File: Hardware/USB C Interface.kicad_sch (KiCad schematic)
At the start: 5 parts

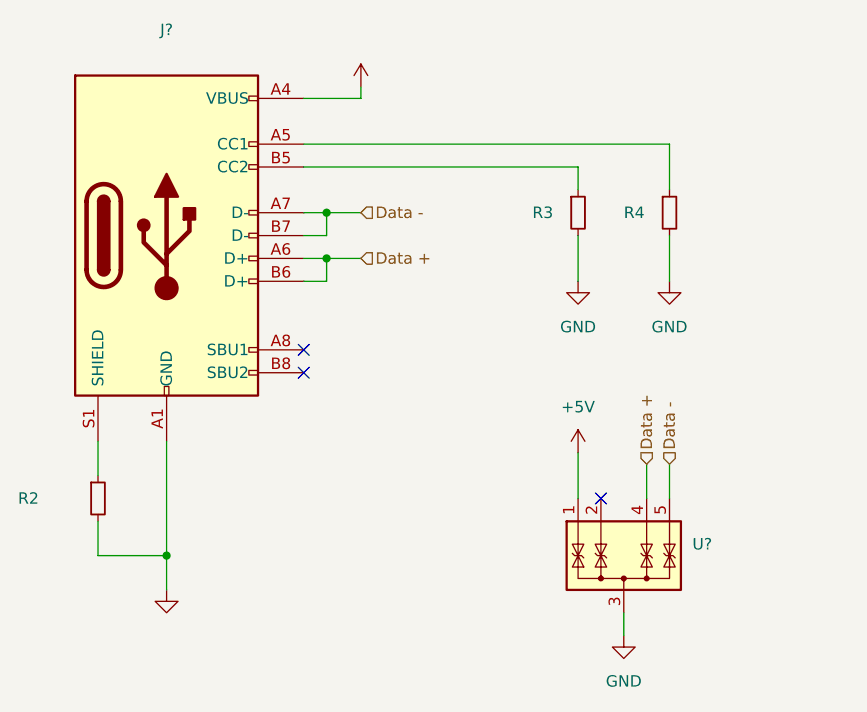
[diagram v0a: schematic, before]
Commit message: Add VL53L0X
Added VL53L0X range finders and reworked traces.
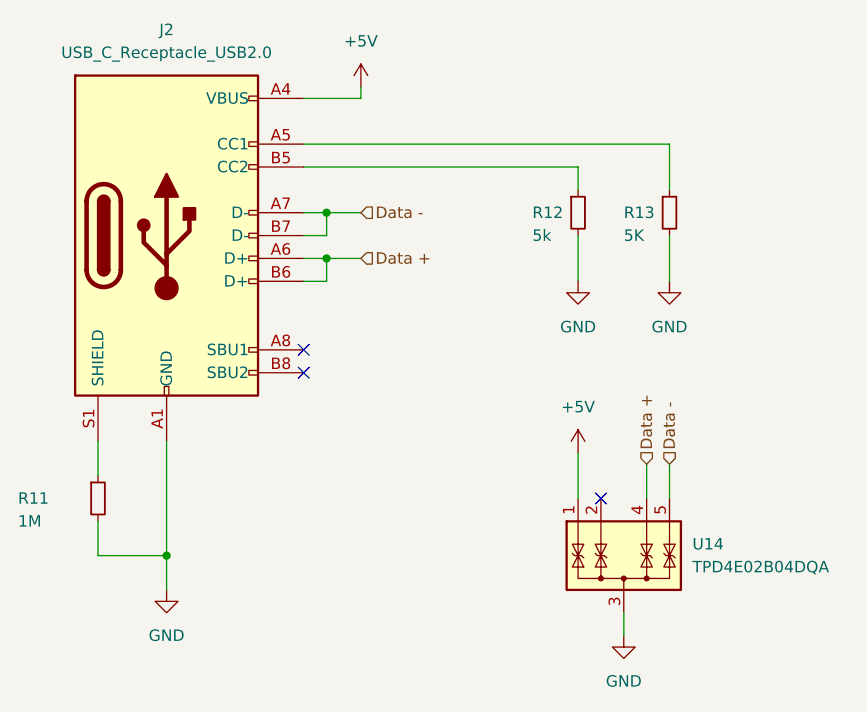
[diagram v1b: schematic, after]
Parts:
- J2: renamed from J?; value (none) -> USB_C_Receptacle_USB2.0; footprint (none) -> Connector_USB:USB_C_Receptacle_XKB_U262-16XN-4BVC11
- R11: renamed from R2; value (none) -> 1M; footprint (none) -> Resistor_SMD:R_0805_2012Metric
- R12: renamed from R3; value (none) -> 5k; footprint (none) -> Resistor_SMD:R_0805_2012Metric
- R13: renamed from R4; value (none) -> 5K; footprint (none) -> Resistor_SMD:R_0805_2012Metric
- U14: renamed from U?; value (none) -> TPD4E02B04DQA; footprint (none) -> Package_SON:USON-10_2.5x1.0mm_P0.5mm
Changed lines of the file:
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@@
   (symbol (lib_id "power:GND") (at 127 130.81 0) (unit 1)
     (in_bom yes) (on_board yes) (fields_autoplaced)
-    (property "Reference" "#PWR?" (id 0) (at 127 137.16 0)
+    (property "Reference" "#PWR059" (id 0) (at 127 137.16 0)
       (effects (font (size 1.27 1.27)) hide)
     )
-    (property "Value" "" (id 1) (at 127 135.89 0))
+    (property "Value" "GND" (id 1) (at 127 135.89 0))
     (property "Footprint" "" (id 2) (at 127 130.81 0)
       (effects (font (size 1.27 1.27)) hide)
@@
   (symbol (lib_id "Device:R_Small") (at 119.38 120.65 0) (unit 1)
     (in_bom yes) (on_board yes)
-    (property "Reference" "R2" (id 0) (at 110.49 120.65 0)
+    (property "Reference" "R11" (id 0) (at 110.49 120.65 0)
       (effects (font (size 1.27 1.27)) (justify left))
     )
-    (property "Value" "" (id 1) (at 110.49 123.19 0)
+    (property "Value" "1M" (id 1) (at 110.49 123.19 0)
       (effects (font (size 1.27 1.27)) (justify left))
     )
-    (property "Footprint" "" (id 2) (at 119.38 120.65 0)
+    (property "Footprint" "Resistor_SMD:R_0805_2012Metric" (id 2) (at 119.38 120.65 0)
       (effects (font (size 1.27 1.27)) hide)
     )
@@
   (symbol (lib_id "Device:R_Small") (at 172.72 88.9 0) (unit 1)
     (in_bom yes) (on_board yes)
-    (property "Reference" "R3" (id 0) (at 167.64 88.9 0)
+    (property "Reference" "R12" (id 0) (at 167.64 88.9 0)
       (effects (font (size 1.27 1.27)) (justify left))
     )
-    (property "Value" "" (id 1) (at 167.64 91.44 0)
+    (property "Value" "5k" (id 1) (at 167.64 91.44 0)
       (effects (font (size 1.27 1.27)) (justify left))
     )
-    (property "Footprint" "" (id 2) (at 172.72 88.9 0)
+    (property "Footprint" "Resistor_SMD:R_0805_2012Metric" (id 2) (at 172.72 88.9 0)
       (effects (font (size 1.27 1.27)) hide)
     )
@@
   (symbol (lib_id "power:GND") (at 172.72 96.52 0) (unit 1)
     (in_bom yes) (on_board yes) (fields_autoplaced)
-    (property "Reference" "#PWR?" (id 0) (at 172.72 102.87 0)
+    (property "Reference" "#PWR061" (id 0) (at 172.72 102.87 0)
       (effects (font (size 1.27 1.27)) hide)
     )
@@
   (symbol (lib_id "power:+5V") (at 148.59 74.93 0) (unit 1)
     (in_bom yes) (on_board yes) (fields_autoplaced)
-    (property "Reference" "#PWR?" (id 0) (at 148.59 78.74 0)
+    (property "Reference" "#PWR060" (id 0) (at 148.59 78.74 0)
       (effects (font (size 1.27 1.27)) hide)
     )
-    (property "Value" "" (id 1) (at 148.59 69.85 0))
+    (property "Value" "+5V" (id 1) (at 148.59 69.85 0))
     (property "Footprint" "" (id 2) (at 148.59 74.93 0)
       (effects (font (size 1.27 1.27)) hide)
@@
   (symbol (lib_id "Power_Protection:TPD4E02B04DQA") (at 177.8 128.27 0) (unit 1)
     (in_bom yes) (on_board yes) (fields_autoplaced)
-    (property "Reference" "U?" (id 0) (at 185.42 125.7299 0)
+    (property "Reference" "U14" (id 0) (at 185.42 125.7299 0)
       (effects (font (size 1.27 1.27)) (justify left))
     )
-    (property "Value" "" (id 1) (at 185.42 128.2699 0)
+    (property "Value" "TPD4E02B04DQA" (id 1) (at 185.42 128.2699 0)
       (effects (font (size 1.27 1.27)) (justify left))
     )
-    (property "Footprint" "" (id 2) (at 185.42 128.27 0)
+    (property "Footprint" "Package_SON:USON-10_2.5x1.0mm_P0.5mm" (id 2) (at 185.42 128.27 0)
       (effects (font (size 1.27 1.27)) (justify left) hide)
     )
@@
   (symbol (lib_id "power:GND") (at 182.88 96.52 0) (unit 1)
     (in_bom yes) (on_board yes) (fields_autoplaced)
-    (property "Reference" "#PWR?" (id 0) (at 182.88 102.87 0)
+    (property "Reference" "#PWR064" (id 0) (at 182.88 102.87 0)
       (effects (font (size 1.27 1.27)) hide)
     )
@@
   (symbol (lib_id "Device:R_Small") (at 182.88 88.9 0) (unit 1)
     (in_bom yes) (on_board yes)
-    (property "Reference" "R4" (id 0) (at 177.8 88.9 0)
+    (property "Reference" "R13" (id 0) (at 177.8 88.9 0)
       (effects (font (size 1.27 1.27)) (justify left))
     )
-    (property "Value" "" (id 1) (at 177.8 91.44 0)
+    (property "Value" "5K" (id 1) (at 177.8 91.44 0)
       (effects (font (size 1.27 1.27)) (justify left))
     )
-    (property "Footprint" "" (id 2) (at 182.88 88.9 0)
+    (property "Footprint" "Resistor_SMD:R_0805_2012Metric" (id 2) (at 182.88 88.9 0)
       (effects (font (size 1.27 1.27)) hide)
     )
@@
   (symbol (lib_id "power:+5V") (at 172.72 115.57 0) (unit 1)
     (in_bom yes) (on_board yes) (fields_autoplaced)
-    (property "Reference" "#PWR?" (id 0) (at 172.72 119.38 0)
+    (property "Reference" "#PWR062" (id 0) (at 172.72 119.38 0)
       (effects (font (size 1.27 1.27)) hide)
     )
@@
   (symbol (lib_id "power:GND") (at 177.8 135.89 0) (unit 1)
     (in_bom yes) (on_board yes) (fields_autoplaced)
-    (property "Reference" "#PWR?" (id 0) (at 177.8 142.24 0)
+    (property "Reference" "#PWR063" (id 0) (at 177.8 142.24 0)
       (effects (font (size 1.27 1.27)) hide)
     )
@@
   (symbol (lib_id "Connector:USB_C_Receptacle_USB2.0") (at 127 91.44 0) (unit 1)
     (in_bom yes) (on_board yes) (fields_autoplaced)
-    (property "Reference" "J?" (id 0) (at 127 68.58 0))
-    (property "Value" "" (id 1) (at 127 71.12 0))
-    (property "Footprint" "" (id 2) (at 130.81 91.44 0)
+    (property "Reference" "J2" (id 0) (at 127 68.58 0))
+    (property "Value" "USB_C_Receptacle_USB2.0" (id 1) (at 127 71.12 0))
+    (property "Footprint" "Connector_USB:USB_C_Receptacle_XKB_U262-16XN-4BVC11" (id 2) (at 130.81 91.44 0)
       (effects (font (size 1.27 1.27)) hide)
     )

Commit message: BIG Changes
Create a 4 Layer Variation
Change Motor Controller routing.
Change Power Regulation.
Optimize Sensor routing.
Pray I know what i'm doing
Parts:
- J2: footprint Connector_USB:USB_C_Receptacle_XKB_U262-16XN-4BVC11 -> Connector_USB:USB_C_Receptacle_GCT_USB4110
- R11, R12, R13: footprint Resistor_SMD:R_0805_2012Metric -> Resistor_SMD:R_0603_1608Metric

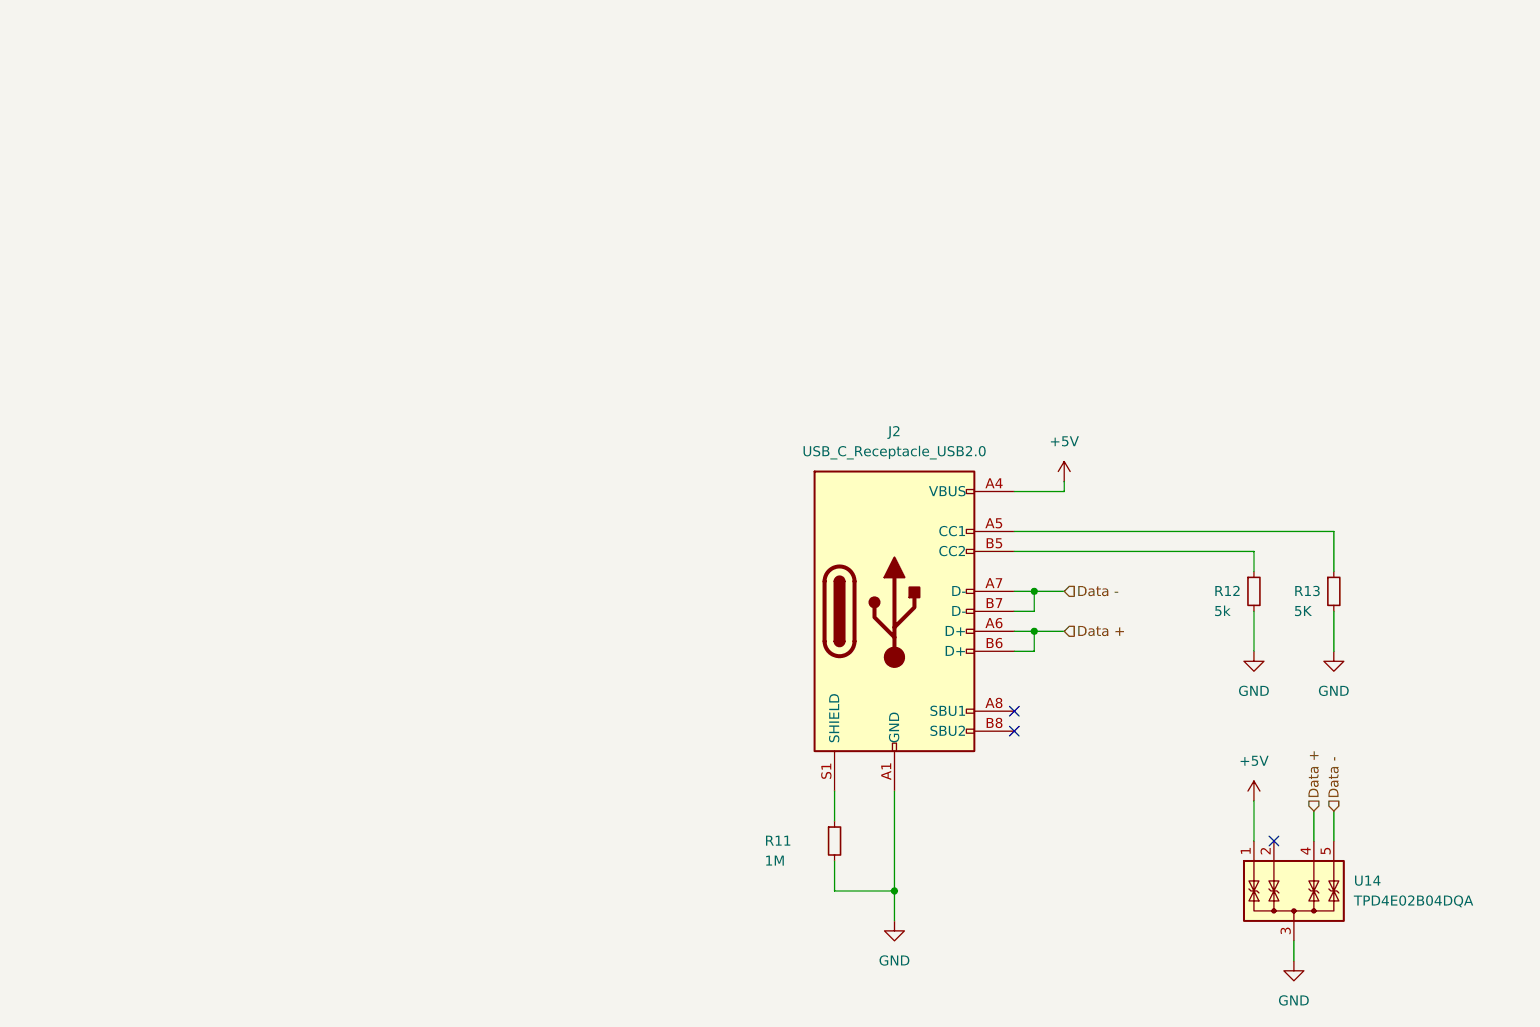
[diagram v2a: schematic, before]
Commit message: 4 L:ayer Board with USB-C
Created a 4-Layer PCB with USB-C updates
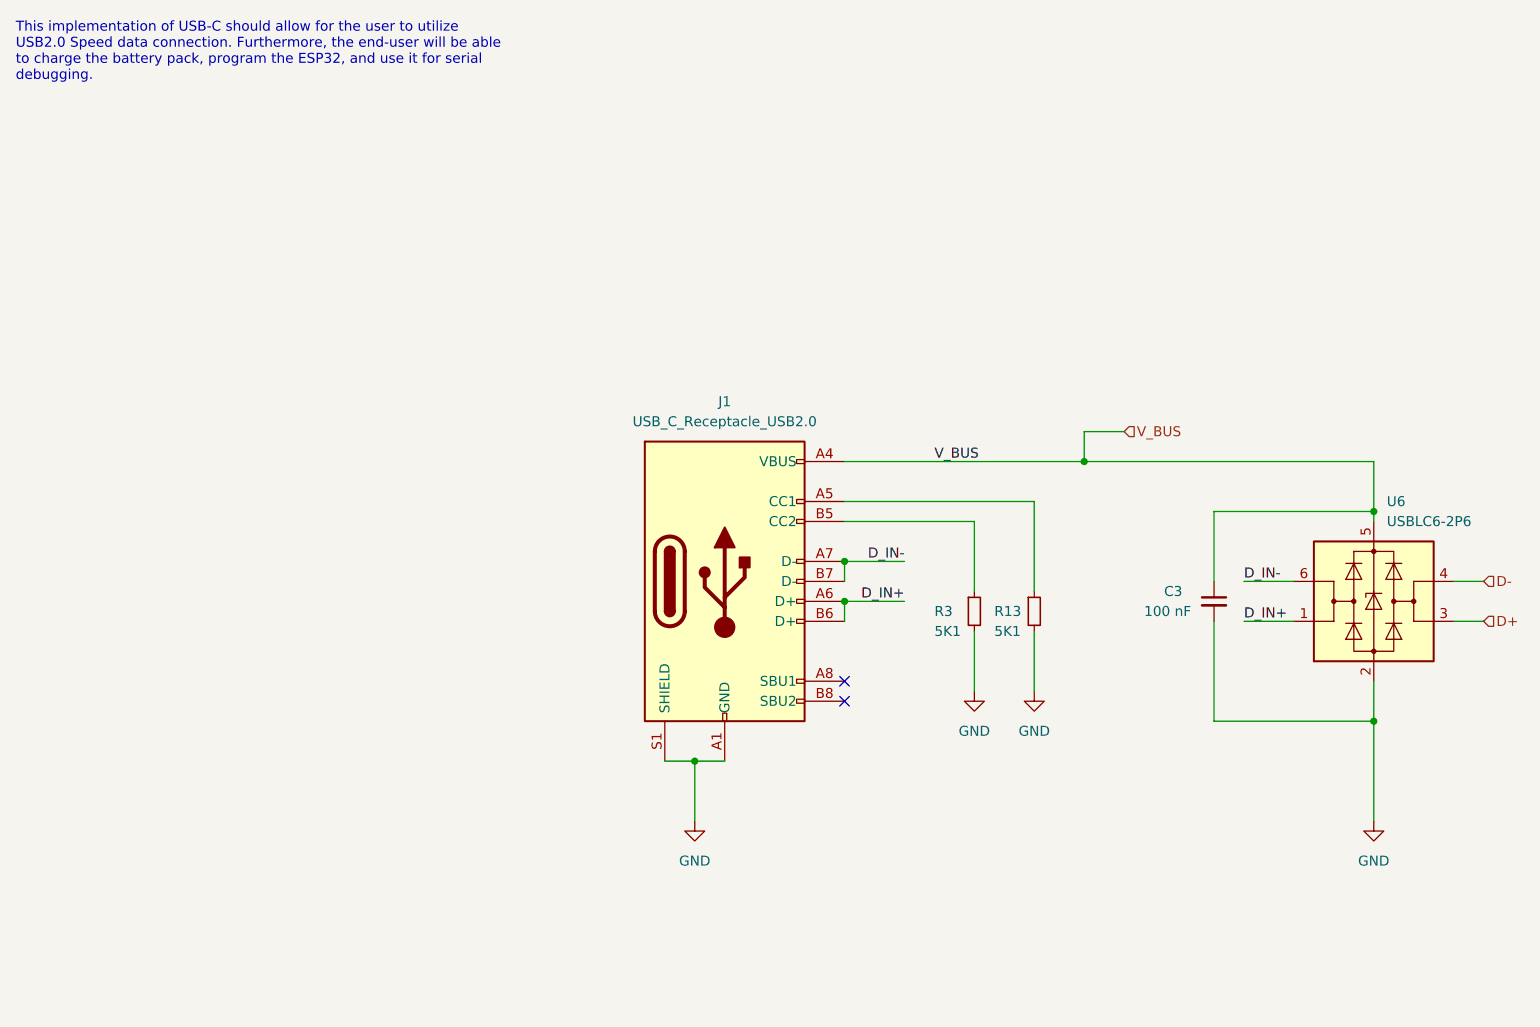
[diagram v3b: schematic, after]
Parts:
- removed J2: USB_C_Receptacle_USB2.0, Connector_USB:USB_C_Receptacle_GCT_USB4110, symbol Connector:USB_C_Receptacle_USB2.0
- removed R11: 1M, Resistor_SMD:R_0603_1608Metric, symbol Device:R_Small
- removed R12: 5k, Resistor_SMD:R_0603_1608Metric, symbol Device:R_Small
- removed U14: TPD4E02B04DQA, Package_SON:USON-10_2.5x1.0mm_P0.5mm, symbol Power_Protection:TPD4E02B04DQA
- added C3: 100 nF, Capacitor_SMD:C_0603_1608Metric, symbol Device:C_Small
- added J1: USB_C_Receptacle_USB2.0, Amoskeag_KiCAD_Lib:GCT_USB4110GFA, symbol Connector:USB_C_Receptacle_USB2.0
- added R3: 5K1, Resistor_SMD:R_0603_1608Metric, symbol Device:R_Small
- added U6: USBLC6-2P6, Package_TO_SOT_SMD:SOT-666, symbol Power_Protection:USBLC6-2P6
- R13: value 5K -> 5K1
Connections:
- net GND: now also C3.2, J1.A1 (GND), J1.A12 (GND), J1.B1 (GND), J1.B12 (GND), J1.S1 (SHIELD), R3.2, U6.2 (GND)
- net at R13.1: now also J1.A5 (CC1)
- new net: J1.B5 (CC2), R3.1
- new net D+: U6.3 (I/O2)
- new net D-: U6.4 (I/O2)
- new net D_IN+: J1.A6 (D+), J1.B6 (D+), U6.1 (I/O1)
- new net D_IN-: J1.A7 (D-), J1.B7 (D-), U6.6 (I/O1)
- new net V_BUS: C3.1, J1.A4 (VBUS), J1.A9 (VBUS), J1.B4 (VBUS), J1.B9 (VBUS), U6.5 (VBUS)
- no-connect marks 3 -> 2
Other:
- note added: "This implementation of USB-C should allow for the user to utilize USB2.0 Speed data connection. Furthermore, the end-user will be able to charge the battery pack, program the ESP32, and use it for serial debugging."
- moved on the sheet: R13

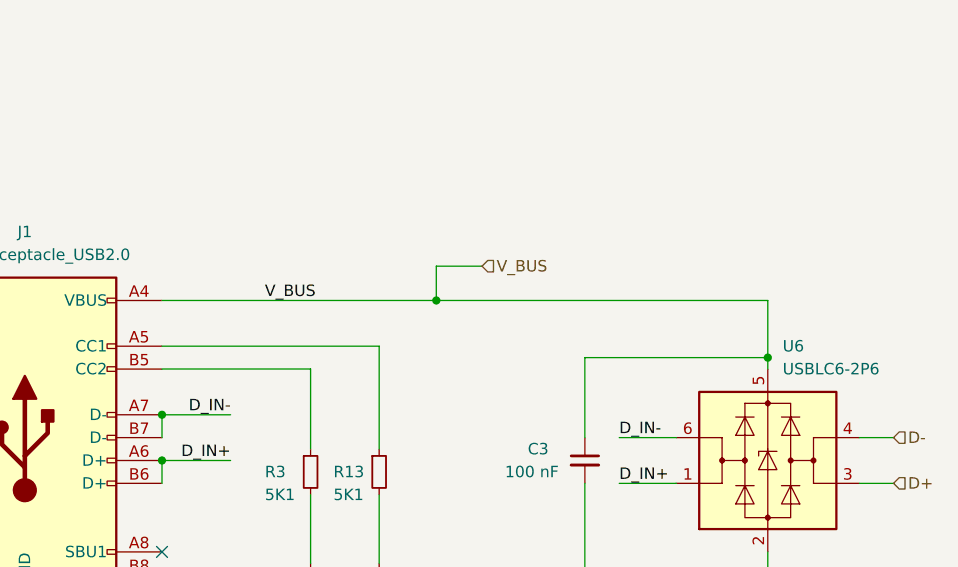
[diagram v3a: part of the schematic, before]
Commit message: Square Board Time
Rerouting, restarting project, trying to make a simpler dev board. Lets see what we can do.
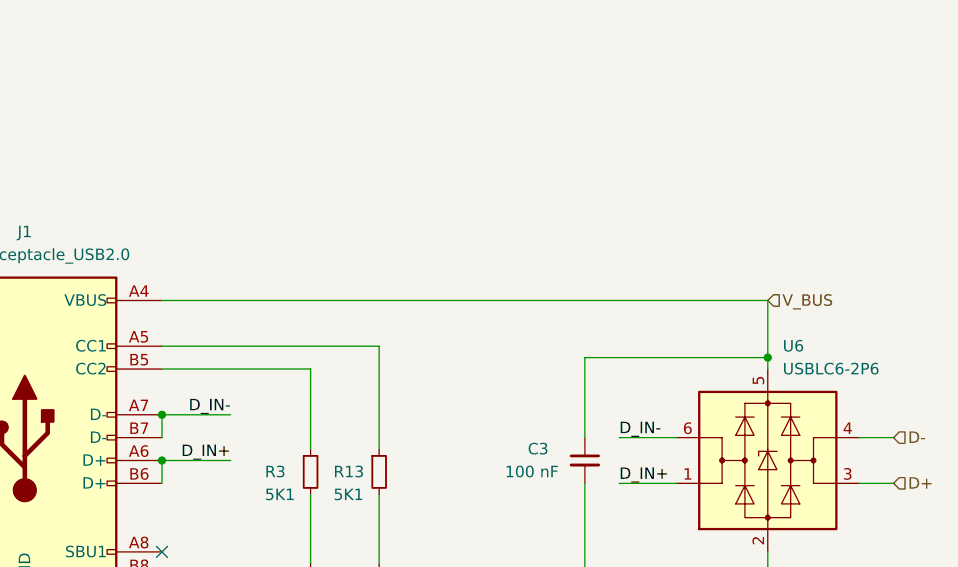
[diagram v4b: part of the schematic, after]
